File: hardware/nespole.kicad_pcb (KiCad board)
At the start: 2 copper layers, 87.9 x 54.9 mm, 48 parts, among them IC1 ATMEGA328PB-A, J1 Screw_Terminal_1x02, J2 Screw_Terminal_1x02, J3 Screw_Terminal_1x05, J4 Screw_Terminal_1x02, J5 Screw_Terminal_1x02, P1 USB_OTG, Q1 MJE13009G, Q2 MOSFET_P_CH, SW1 Rotary_Encoder_Switch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

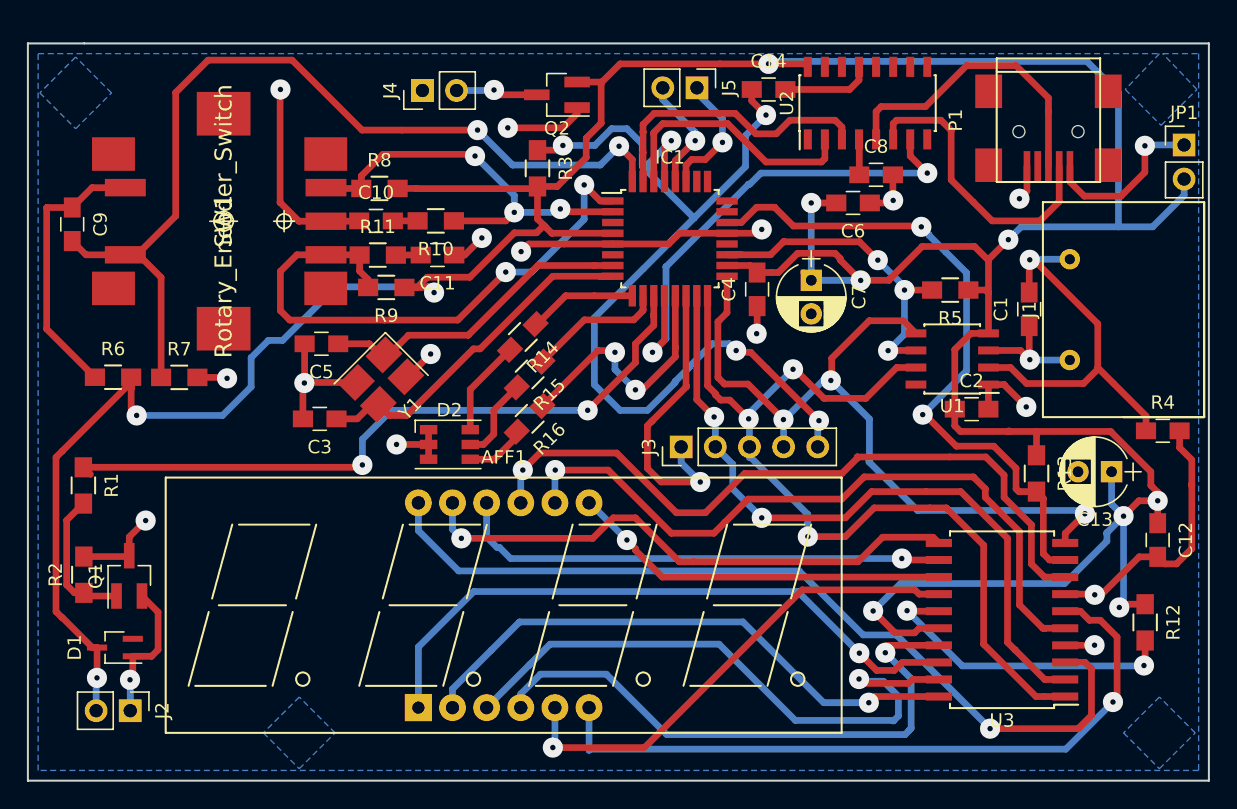
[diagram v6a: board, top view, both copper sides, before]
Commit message: Updating hardware to correct for...mistakes; finishing-up software.
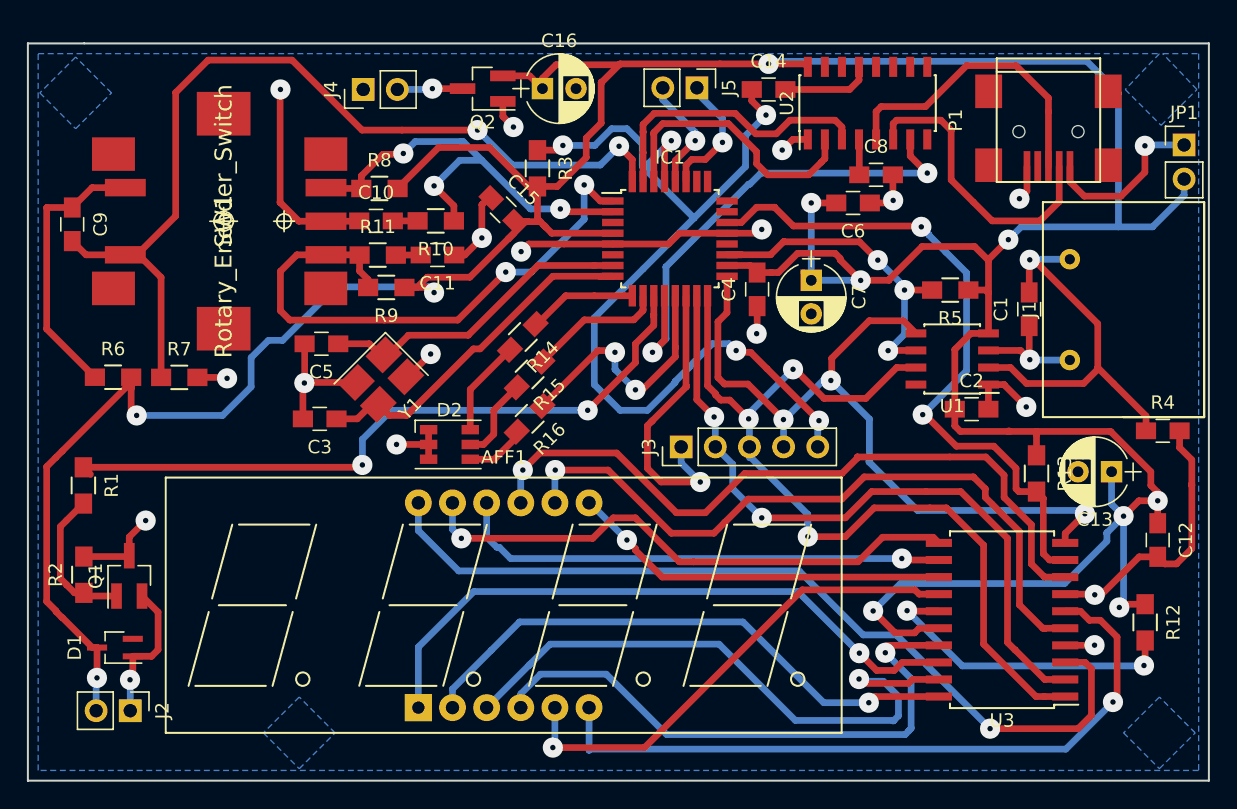
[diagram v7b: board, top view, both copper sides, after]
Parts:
- added C15: 0.1u, Capacitors_SMD:C_0805_HandSoldering, F.Cu at (140.0, 113.2)
- added C16: 22m, Capacitors_THT:CP_Radial_D5.0mm_P2.50mm, F.Cu at (142.9, 104.2)
- C7: value 22m -> 10m
- R14, R15: value ? -> 1k
- R16: value ? -> 1.5k
- moved Q2 5.54 mm to (138.5, 104.2)
- moved J4 4.41 mm to (129.6, 104.3)
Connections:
- net Net-(AFF1-Pad1) renamed /LED_SEGMENT_E
- net Net-(AFF1-Pad10) renamed /LED_SEGMENT_F
- net Net-(AFF1-Pad11) renamed /LED_SEGMENT_A
- net Net-(AFF1-Pad12) renamed /LED_DIGIT_0
- net Net-(AFF1-Pad2) renamed /LED_SEGMENT_D
- net Net-(AFF1-Pad3) renamed /LED_SEGMENT_DP
- net Net-(AFF1-Pad4) renamed /LED_SEGMENT_C
- net Net-(AFF1-Pad5) renamed /LED_SEGMENT_G
- net Net-(AFF1-Pad6) renamed /LED_DIGIT_3
- net Net-(AFF1-Pad7) renamed /LED_SEGMENT_B
- net Net-(AFF1-Pad8) renamed /LED_DIGIT_2
- net Net-(AFF1-Pad9) renamed /LED_DIGIT_1
- IC1 pad 13: LED_B -> LED_R
- IC1 pad 9: LED_R -> LED_B
- R14 pad 1: LED_R -> LED_B
- R16 pad 1: LED_B -> LED_R
- U2 pad 1: Net-(U2-Pad1) -> GND
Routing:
- net +5V: track 293.6 -> 307.2 mm
- net LED_R: track 8.07 -> 19.3 mm, vias 0 -> 2
- net LED_B: track 19.3 -> 8.07 mm, vias 2 -> 0
- net SW_DIR: track 30.5 -> 33.5 mm
- net GND: track 104.1 -> 105.9 mm, vias 16 -> 17
- net RXD: track 19.4 -> 20.7 mm
- net Net-(J4-Pad2): track 6.13 -> 4.88 mm

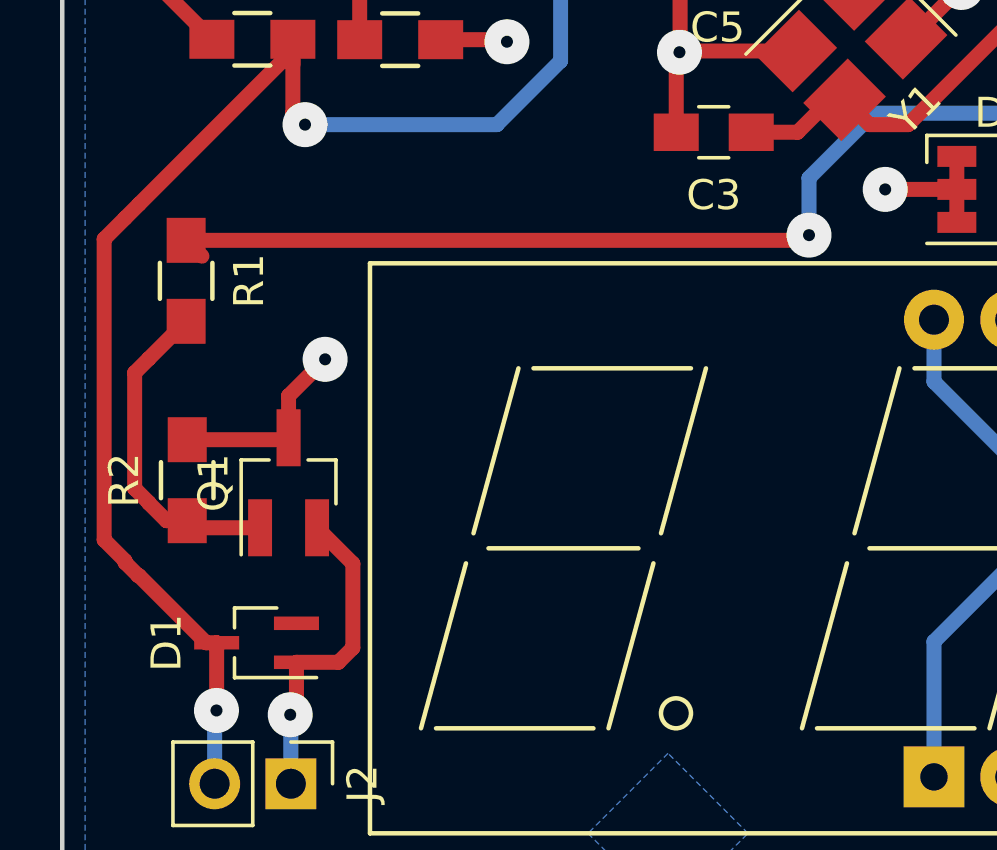
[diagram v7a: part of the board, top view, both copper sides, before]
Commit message: Fully-working; fixed schematic to wire the mosfet properly.
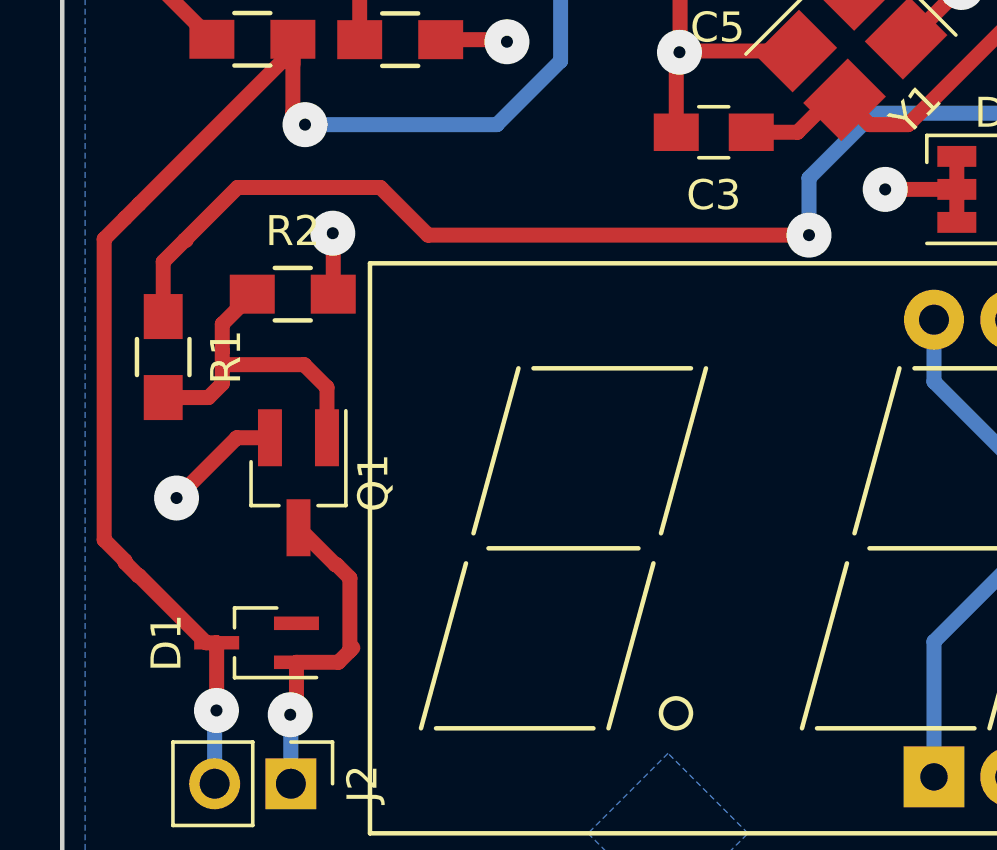
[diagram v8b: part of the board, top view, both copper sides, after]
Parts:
- Q1: value MJE13009G -> MOSFET_N_CH; footprint TO_SOT_Packages_SMD:SOT-23_Handsoldering -> nespole:SOT-23_Handsoldering
- moved R2 7.13 mm to (112.3, 134.2), turned to 0 degrees
- moved R1 2.65 mm to (108.0, 136.3)
- moved Q1 0.33 mm to (112.5, 140.5), turned to 270 degrees
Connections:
- R1 pad 2: Net-(Q1-Pad1) -> Net-(Q1-PadG)
- R2 pad 1: Net-(Q1-Pad1) -> Net-(Q1-PadG)
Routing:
- net Net-(Q1-PadG): track 0.00 -> 11.0 mm
- net Net-(Q1-Pad1): track 11.0 -> 0.00 mm
- net ENABLE_RELAY: track 52.3 -> 56.0 mm
- net GND: track 105.9 -> 105.4 mm, vias 17 -> 18
